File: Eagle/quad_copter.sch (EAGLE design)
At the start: 12 parts, among them X1 STM32F4_DISC

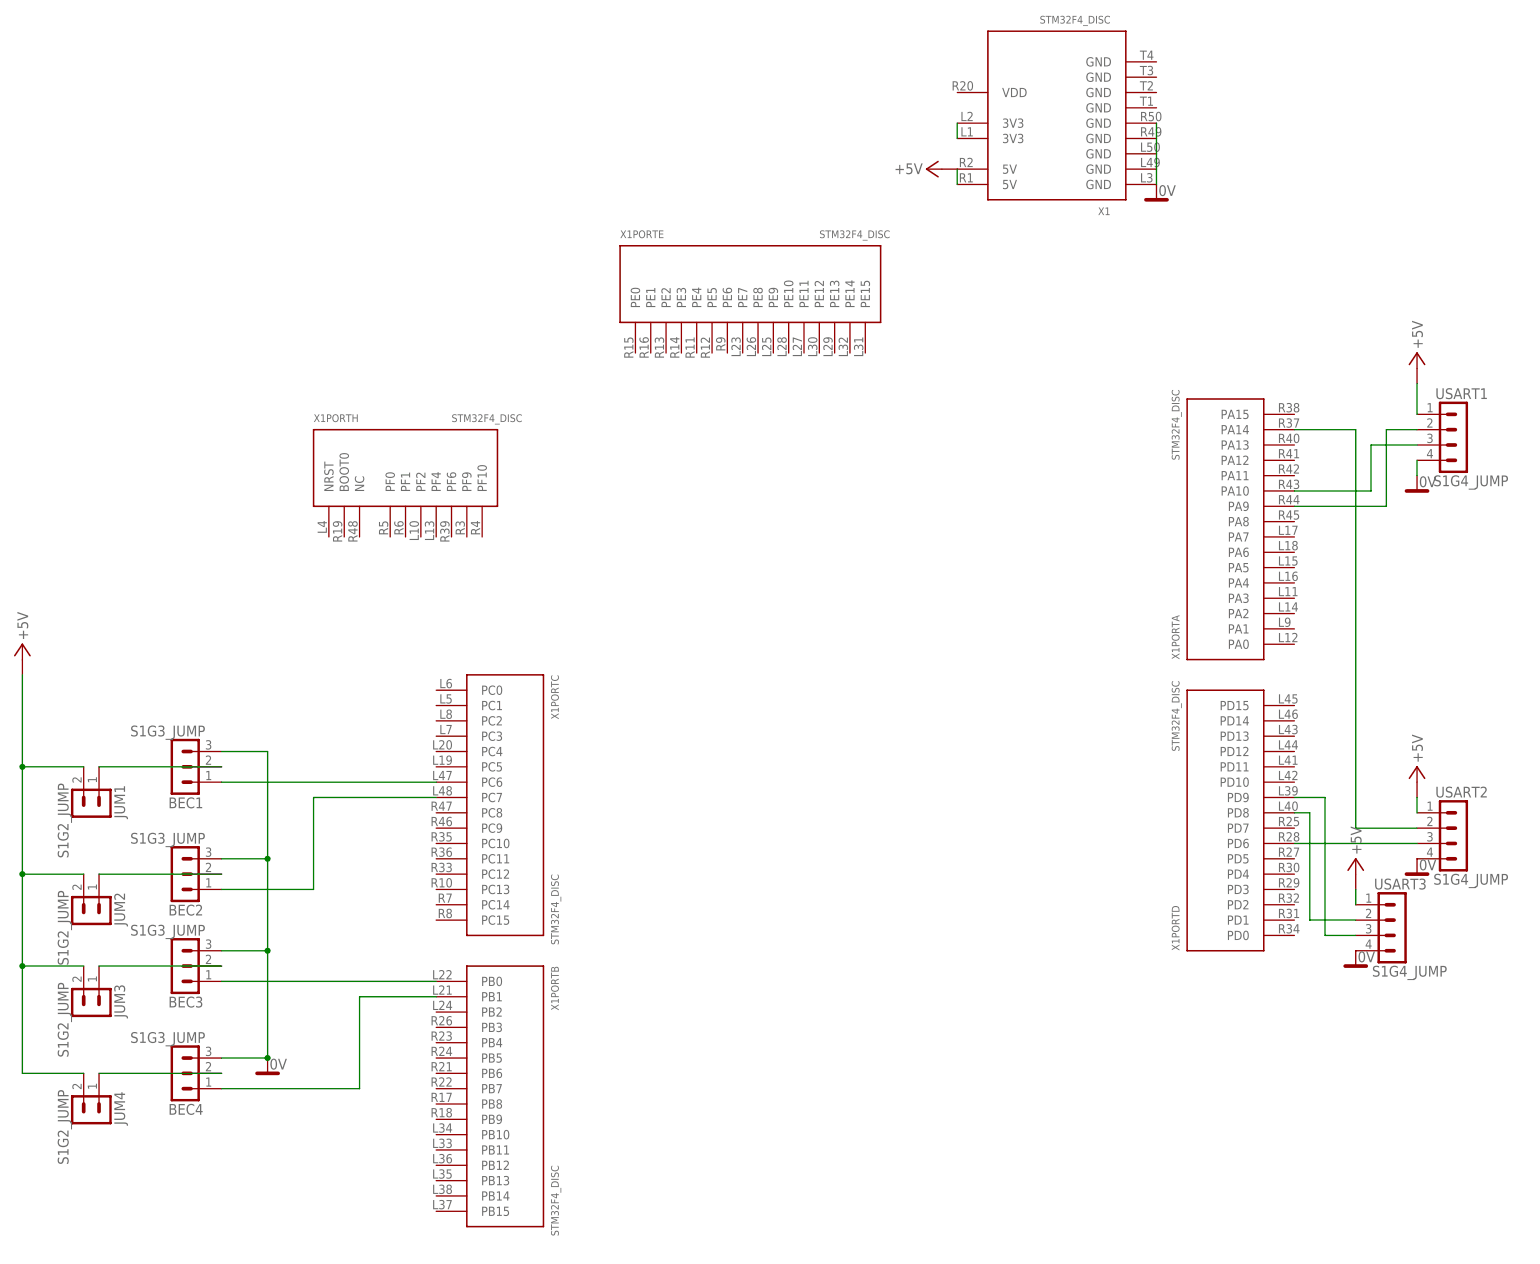
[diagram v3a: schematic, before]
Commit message: Added connector to board
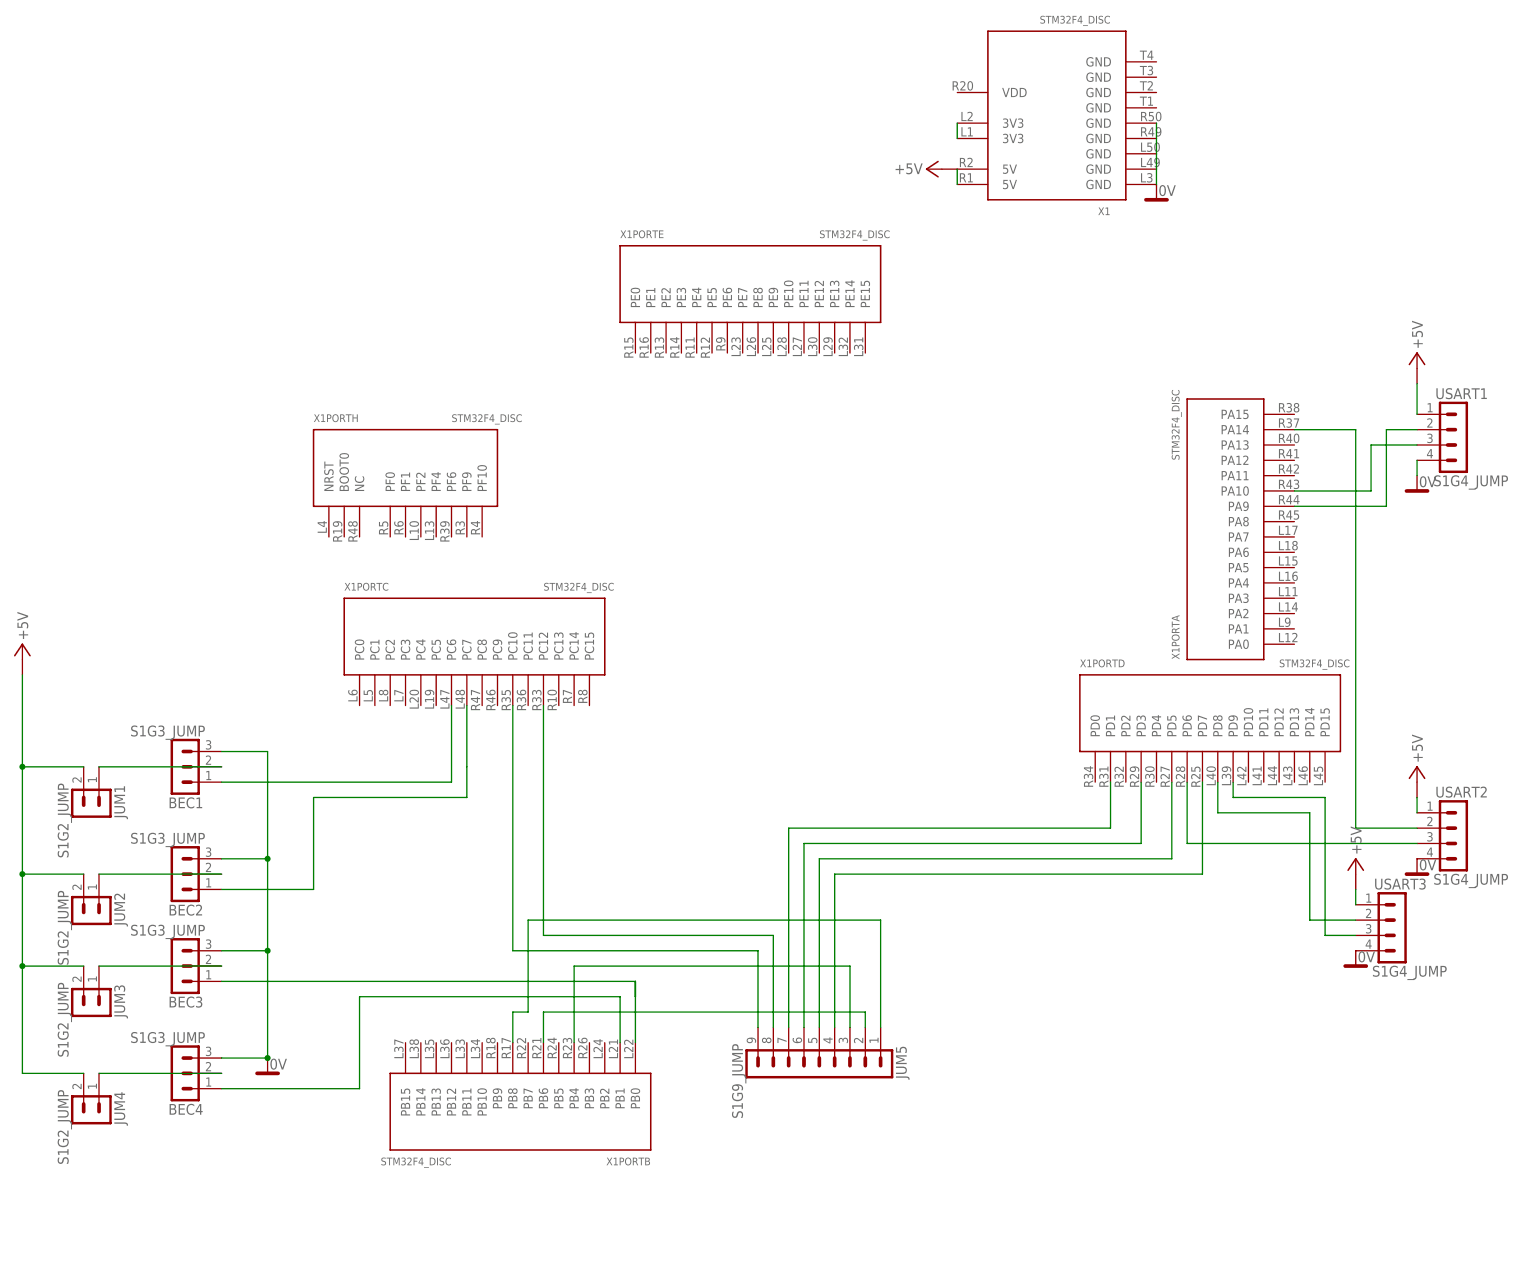
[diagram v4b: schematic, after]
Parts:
- added JUM5: S1G9_JUMP, #PaJa_konektory:S1G9_JUMP
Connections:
- new net N$20: JUM5.9, X1PORTC.PC10
- new net N$21: JUM5.8, X1PORTC.PC12
- new net N$22: JUM5.6, X1PORTD.PD3
- new net N$23: JUM5.5, X1PORTD.PD5
- new net N$24: JUM5.4, X1PORTD.PD7
- new net N$25: JUM5.7, X1PORTD.PD1
- new net N$27: JUM5.3, X1PORTB.PB4
- new net N$28: JUM5.1, X1PORTB.PB8
- new net N$29: JUM5.2, X1PORTB.PB6
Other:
- moved on the sheet: X1PORTB, X1PORTC, X1PORTD
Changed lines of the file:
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@@
 <part name="0V1" library="#PaJa_30" deviceset="0V" device=""/>
 <part name="NAP1" library="#PaJa_30" deviceset="+5V" device=""/>
+<part name="JUM5" library="#PaJa_konektory" deviceset="S1G9_JUMP" device=""/>
 </parts>
 <sheets>
@@
 <instance part="X1" gate="PWR" x="106.68" y="81.28" rot="R90"/>
 <instance part="X1" gate="PORTA" x="134.62" y="10.16" rot="R90"/>
-<instance part="X1" gate="PORTB" x="12.7" y="-81.28" rot="R270"/>
-<instance part="X1" gate="PORTC" x="12.7" y="-33.02" rot="R270"/>
-<instance part="X1" gate="PORTD" x="134.62" y="-38.1" rot="R90"/>
+<instance part="X1" gate="PORTB" x="17.78" y="-83.82" rot="R180"/>
+<instance part="X1" gate="PORTC" x="7.62" y="-7.62"/>
+<instance part="X1" gate="PORTD" x="129.54" y="-20.32"/>
 <instance part="X1" gate="PORTE" x="53.34" y="50.8"/>
 <instance part="X1" gate="PORTH" x="-2.54" y="20.32"/>
@@
 <instance part="0V1" gate="0" x="154.94" y="-60.96"/>
 <instance part="NAP1" gate="+5" x="154.94" y="-43.18"/>
+<instance part="JUM5" gate="JUM" x="66.04" y="-73.66" rot="R180"/>
 </instances>
 <busses>
@@
 <wire x1="-10.16" y1="-81.28" x2="-10.16" y2="-66.04" width="0.1524" layer="91"/>
 <pinref part="X1" gate="PORTB" pin="PB1"/>
-<wire x1="-10.16" y1="-66.04" x2="2.54" y2="-66.04" width="0.1524" layer="91"/>
+<wire x1="-10.16" y1="-66.04" x2="33.02" y2="-66.04" width="0.1524" layer="91"/>
+<wire x1="33.02" y1="-66.04" x2="33.02" y2="-73.66" width="0.1524" layer="91"/>
 </segment>
 </net>
@@
 <pinref part="BEC3" gate="JUMP" pin="1"/>
 <pinref part="X1" gate="PORTB" pin="PB0"/>
-<wire x1="-33.02" y1="-63.5" x2="2.54" y2="-63.5" width="0.1524" layer="91"/>
+<wire x1="-33.02" y1="-63.5" x2="35.56" y2="-63.5" width="0.1524" layer="91"/>
+<wire x1="35.56" y1="-63.5" x2="35.56" y2="-66.04" width="0.1524" layer="91"/>
+<wire x1="35.56" y1="-66.04" x2="35.56" y2="-63.5" width="0.1524" layer="91"/>
+<wire x1="35.56" y1="-63.5" x2="35.56" y2="-66.04" width="0.1524" layer="91"/>
+<wire x1="35.56" y1="-66.04" x2="35.56" y2="-73.66" width="0.1524" layer="91"/>
 </segment>
 </net>
@@
 <wire x1="-17.78" y1="-48.26" x2="-17.78" y2="-33.02" width="0.1524" layer="91"/>
 <pinref part="X1" gate="PORTC" pin="PC7"/>
-<wire x1="-17.78" y1="-33.02" x2="2.54" y2="-33.02" width="0.1524" layer="91"/>
+<wire x1="-17.78" y1="-33.02" x2="7.62" y2="-33.02" width="0.1524" layer="91"/>
+<wire x1="7.62" y1="-33.02" x2="7.62" y2="-27.94" width="0.1524" layer="91"/>
+<wire x1="7.62" y1="-27.94" x2="7.62" y2="-17.78" width="0.1524" layer="91"/>
 </segment>
 </net>
@@
 <segment>
 <pinref part="BEC1" gate="JUMP" pin="1"/>
-<wire x1="-33.02" y1="-30.48" x2="2.54" y2="-30.48" width="0.1524" layer="91"/>
+<wire x1="-33.02" y1="-30.48" x2="5.08" y2="-30.48" width="0.1524" layer="91"/>
+<wire x1="5.08" y1="-30.48" x2="5.08" y2="-17.78" width="0.1524" layer="91"/>
 <pinref part="X1" gate="PORTC" pin="PC6"/>
 </segment>
@@
 <pinref part="USART2" gate="JUMP" pin="3"/>
 <pinref part="X1" gate="PORTD" pin="PD6"/>
-<wire x1="165.1" y1="-40.64" x2="144.78" y2="-40.64" width="0.1524" layer="91"/>
+<wire x1="165.1" y1="-40.64" x2="127" y2="-40.64" width="0.1524" layer="91"/>
+<wire x1="127" y1="-40.64" x2="127" y2="-30.48" width="0.1524" layer="91"/>
 </segment>
 </net>
@@
 <segment>
 <pinref part="X1" gate="PORTD" pin="PD9"/>
-<wire x1="144.78" y1="-33.02" x2="149.86" y2="-33.02" width="0.1524" layer="91"/>
+<wire x1="134.62" y1="-30.48" x2="134.62" y2="-33.02" width="0.1524" layer="91"/>
+<wire x1="134.62" y1="-33.02" x2="149.86" y2="-33.02" width="0.1524" layer="91"/>
 <wire x1="149.86" y1="-33.02" x2="149.86" y2="-55.88" width="0.1524" layer="91"/>
 <pinref part="USART3" gate="JUMP" pin="3"/>
@@
 <wire x1="147.32" y1="-53.34" x2="147.32" y2="-35.56" width="0.1524" layer="91"/>
 <pinref part="X1" gate="PORTD" pin="PD8"/>
-<wire x1="147.32" y1="-35.56" x2="144.78" y2="-35.56" width="0.1524" layer="91"/>
-</segment>
-</net>
+<wire x1="147.32" y1="-35.56" x2="132.08" y2="-35.56" width="0.1524" layer="91"/>
+<wire x1="132.08" y1="-35.56" x2="132.08" y2="-30.48" width="0.1524" layer="91"/>
+</segment>
+</net>
+<net name="N$20" class="0">
+<segment>
+<pinref part="X1" gate="PORTC" pin="PC10"/>
+<wire x1="15.24" y1="-17.78" x2="15.24" y2="-58.42" width="0.1524" layer="91"/>
+<wire x1="15.24" y1="-58.42" x2="55.88" y2="-58.42" width="0.1524" layer="91"/>
+<wire x1="55.88" y1="-58.42" x2="55.88" y2="-71.12" width="0.1524" layer="91"/>
+<pinref part="JUM5" gate="JUM" pin="9"/>
+</segment>
+</net>
+<net name="N$21" class="0">
+<segment>
+<pinref part="X1" gate="PORTC" pin="PC12"/>
+<wire x1="20.32" y1="-17.78" x2="20.32" y2="-55.88" width="0.1524" layer="91"/>
+<wire x1="20.32" y1="-55.88" x2="58.42" y2="-55.88" width="0.1524" layer="91"/>
+<wire x1="58.42" y1="-55.88" x2="58.42" y2="-71.12" width="0.1524" layer="91"/>
+<pinref part="JUM5" gate="JUM" pin="8"/>
+</segment>
+</net>
+<net name="N$22" class="0">
+<segment>
+<pinref part="X1" gate="PORTD" pin="PD3"/>
+<wire x1="119.38" y1="-40.64" x2="119.38" y2="-30.48" width="0.1524" layer="91"/>
+<wire x1="119.38" y1="-40.64" x2="63.5" y2="-40.64" width="0.1524" layer="91"/>
+<wire x1="63.5" y1="-40.64" x2="63.5" y2="-71.12" width="0.1524" layer="91"/>
+<pinref part="JUM5" gate="JUM" pin="6"/>
+</segment>
+</net>
+<net name="N$23" class="0">
+<segment>
+<pinref part="X1" gate="PORTD" pin="PD5"/>
+<wire x1="124.46" y1="-30.48" x2="124.46" y2="-43.18" width="0.1524" layer="91"/>
+<wire x1="124.46" y1="-43.18" x2="66.04" y2="-43.18" width="0.1524" layer="91"/>
+<wire x1="66.04" y1="-43.18" x2="66.04" y2="-71.12" width="0.1524" layer="91"/>
+<pinref part="JUM5" gate="JUM" pin="5"/>
+</segment>
+</net>
+<net name="N$24" class="0">
+<segment>
+<pinref part="X1" gate="PORTD" pin="PD7"/>
+<wire x1="129.54" y1="-30.48" x2="129.54" y2="-45.72" width="0.1524" layer="91"/>
+<wire x1="129.54" y1="-45.72" x2="68.58" y2="-45.72" width="0.1524" layer="91"/>
+<wire x1="68.58" y1="-45.72" x2="68.58" y2="-71.12" width="0.1524" layer="91"/>
+<pinref part="JUM5" gate="JUM" pin="4"/>
+</segment>
+</net>
+<net name="N$25" class="0">
+<segment>
+<pinref part="X1" gate="PORTD" pin="PD1"/>
+<wire x1="114.3" y1="-30.48" x2="114.3" y2="-38.1" width="0.1524" layer="91"/>
+<wire x1="114.3" y1="-38.1" x2="60.96" y2="-38.1" width="0.1524" layer="91"/>
+<wire x1="60.96" y1="-38.1" x2="60.96" y2="-71.12" width="0.1524" layer="91"/>
+<pinref part="JUM5" gate="JUM" pin="7"/>
+</segment>
+</net>
+<net name="N$28" class="0">
+<segment>
+<pinref part="X1" gate="PORTB" pin="PB8"/>
+<wire x1="15.24" y1="-73.66" x2="15.24" y2="-68.58" width="0.1524" layer="91"/>
+<wire x1="15.24" y1="-68.58" x2="17.78" y2="-68.58" width="0.1524" layer="91"/>
+<wire x1="17.78" y1="-68.58" x2="17.78" y2="-53.34" width="0.1524" layer="91"/>
+<wire x1="17.78" y1="-53.34" x2="76.2" y2="-53.34" width="0.1524" layer="91"/>
+<wire x1="76.2" y1="-53.34" x2="76.2" y2="-71.12" width="0.1524" layer="91"/>
+<pinref part="JUM5" gate="JUM" pin="1"/>
+</segment>
+</net>
+<net name="N$27" class="0">
+<segment>
+<pinref part="X1" gate="PORTB" pin="PB4"/>
+<wire x1="25.4" y1="-73.66" x2="25.4" y2="-60.96" width="0.1524" layer="91"/>
+<wire x1="71.12" y1="-71.12" x2="71.12" y2="-60.96" width="0.1524" layer="91"/>
+<wire x1="71.12" y1="-60.96" x2="25.4" y2="-60.96" width="0.1524" layer="91"/>
+<pinref part="JUM5" gate="JUM" pin="3"/>
+</segment>
+</net>
+<net name="N$29" class="0">
+<segment>
+<pinref part="X1" gate="PORTB" pin="PB6"/>
+<wire x1="20.32" y1="-73.66" x2="20.32" y2="-68.58" width="0.1524" layer="91"/>
+<wire x1="20.32" y1="-68.58" x2="73.66" y2="-68.58" width="0.1524" layer="91"/>
+<wire x1="73.66" y1="-68.58" x2="73.66" y2="-71.12" width="0.1524" layer="91"/>
+<pinref part="JUM5" gate="JUM" pin="2"/>
+</segment>
+</net>

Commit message: Screenshots
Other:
- moved on the sheet: X1, X1PORTE, X1PORTH
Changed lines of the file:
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@@
 </plain>
 <instances>
-<instance part="X1" gate="PWR" x="106.68" y="81.28" rot="R90"/>
+<instance part="X1" gate="PWR" x="71.12" y="-5.08" rot="R90"/>
 <instance part="X1" gate="PORTA" x="134.62" y="10.16" rot="R90"/>
 <instance part="X1" gate="PORTB" x="17.78" y="-83.82" rot="R180"/>
 <instance part="X1" gate="PORTC" x="7.62" y="-7.62"/>
 <instance part="X1" gate="PORTD" x="129.54" y="-20.32"/>
-<instance part="X1" gate="PORTE" x="53.34" y="50.8"/>
-<instance part="X1" gate="PORTH" x="-2.54" y="20.32"/>
+<instance part="X1" gate="PORTE" x="50.8" y="66.04"/>
+<instance part="X1" gate="PORTH" x="-15.24" y="66.04"/>
 <instance part="USART1" gate="JUMP" x="167.64" y="27.94" rot="R270"/>
 <instance part="USART2" gate="JUMP" x="167.64" y="-38.1" rot="R270"/>
@@
 <instance part="NAP2" gate="+5" x="165.1" y="40.64"/>
 <instance part="NAP3" gate="+5" x="165.1" y="-27.94"/>
-<instance part="NAP4" gate="+5" x="83.82" y="71.12" rot="R90"/>
-<instance part="0V4" gate="0" x="121.92" y="66.04"/>
+<instance part="NAP4" gate="+5" x="48.26" y="-15.24" rot="R90"/>
+<instance part="0V4" gate="0" x="86.36" y="-20.32"/>
 <instance part="BEC1" gate="JUMP" x="-35.56" y="-27.94" rot="R90"/>
 <instance part="BEC2" gate="JUMP" x="-35.56" y="-45.72" rot="R90"/>
@@
 <pinref part="NAP4" gate="+5" pin="+5V"/>
 <pinref part="X1" gate="PWR" pin="5V@1"/>
-<wire x1="88.9" y1="68.58" x2="88.9" y2="71.12" width="0.1524" layer="91"/>
+<wire x1="53.34" y1="-17.78" x2="53.34" y2="-15.24" width="0.1524" layer="91"/>
 </segment>
 <segment>
@@
 <pinref part="X1" gate="PWR" pin="GND@3"/>
 <pinref part="X1" gate="PWR" pin="GND@2"/>
-<wire x1="121.92" y1="68.58" x2="121.92" y2="71.12" width="0.1524" layer="91"/>
-<wire x1="121.92" y1="71.12" x2="121.92" y2="73.66" width="0.1524" layer="91"/>
+<wire x1="86.36" y1="-17.78" x2="86.36" y2="-15.24" width="0.1524" layer="91"/>
+<wire x1="86.36" y1="-15.24" x2="86.36" y2="-12.7" width="0.1524" layer="91"/>
 <pinref part="X1" gate="PWR" pin="GND@4"/>
 <pinref part="X1" gate="PWR" pin="GND@5"/>
-<wire x1="121.92" y1="76.2" x2="121.92" y2="78.74" width="0.1524" layer="91"/>
-<wire x1="121.92" y1="73.66" x2="121.92" y2="76.2" width="0.1524" layer="91"/>
+<wire x1="86.36" y1="-10.16" x2="86.36" y2="-7.62" width="0.1524" layer="91"/>
+<wire x1="86.36" y1="-12.7" x2="86.36" y2="-10.16" width="0.1524" layer="91"/>
 </segment>
 <segment>
@@
 <pinref part="X1" gate="PWR" pin="3V3@2"/>
 <pinref part="X1" gate="PWR" pin="3V3@1"/>
-<wire x1="88.9" y1="78.74" x2="88.9" y2="76.2" width="0.1524" layer="91"/>
+<wire x1="53.34" y1="-7.62" x2="53.34" y2="-10.16" width="0.1524" layer="91"/>
 </segment>
 </net>
